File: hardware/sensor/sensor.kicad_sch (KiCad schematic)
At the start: 1 part

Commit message: commit to save work from misbehaving laptop
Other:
- sheet BMS renamed P_{IN}
- sheet Microcontroller ports: added enFrontend; removed none
- sheet Sensor ports: added shutdown; removed none
- moved on the sheet: AE1

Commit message: Fix incorrect upstream
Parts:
- removed AE1: Antenna, symbol Device:Antenna
- added J101: Conn_Coaxial, Connector_Coaxial:SMA_Amphenol_901-143_Horizontal, symbol Connector:Conn_Coaxial
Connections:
- net Microcontroller/Antenna: now also J101.1 (In)
- new net GND: J101.2 (Ext)
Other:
- sheet Microcontroller ports: added LDO_{EN}, V_{ref}, {bms-status}; removed EH_{On}, P_{Good}, V_{Ref}, enFrontend
- sheet P_{IN} ports: added LDO_{EN}, LDO_{OUT}, {bms-status}; removed EH_{On}, P_{Good}
- sheet Reference ports: added V_{ref}; removed V_{Ref}
- sheet Sensor ports: added none; removed shutdown

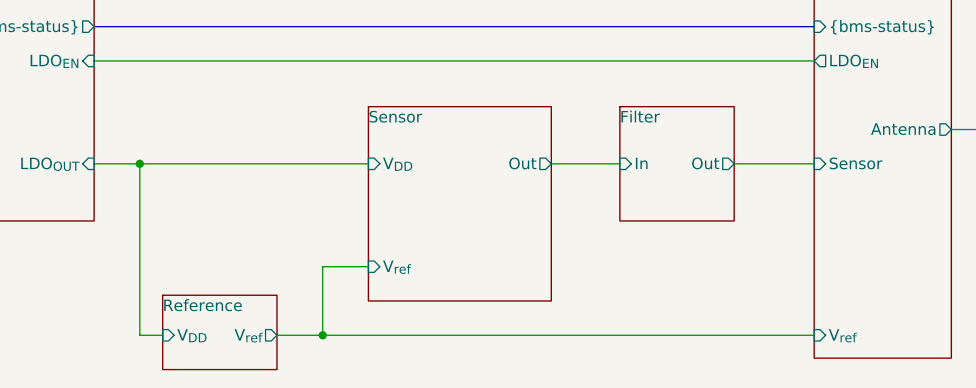
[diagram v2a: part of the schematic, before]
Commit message: Finished initial pcb routing
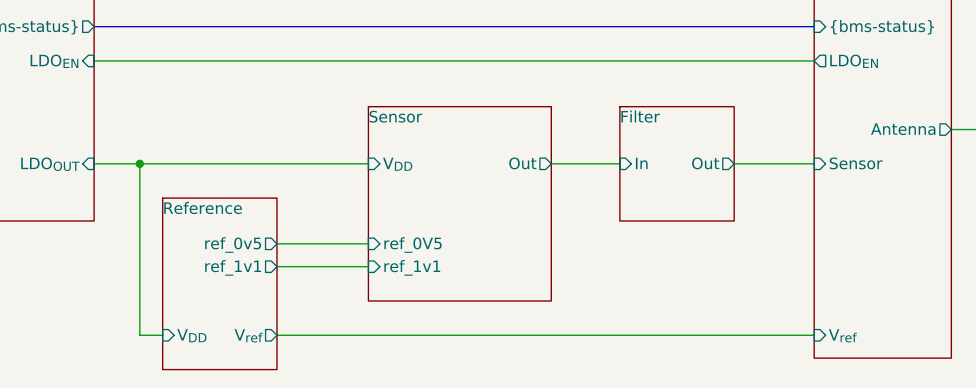
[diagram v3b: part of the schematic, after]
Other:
- sheet Reference ports: added ref_0v5, ref_1v1; removed none
- sheet Sensor ports: added ref_0V5, ref_1v1; removed V_{ref}
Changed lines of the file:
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@@
   (junction (at 59.69 62.23) (diameter 0) (color 0 0 0 0)
-  )
-  (junction (at 80.01 81.28) (diameter 0) (color 0 0 0 0)
   )
   (bus (pts (xy 54.61 46.99) (xy 134.62 46.99))
@@
     (stroke (width 0) (type default))
   )
-  (wire (pts (xy 74.93 81.28) (xy 80.01 81.28))
+  (wire (pts (xy 59.69 62.23) (xy 85.09 62.23))
     (stroke (width 0) (type default))
   )
-  (wire (pts (xy 59.69 62.23) (xy 85.09 62.23))
+  (wire (pts (xy 74.93 81.28) (xy 134.62 81.28))
     (stroke (width 0) (type default))
   )
@@
     (stroke (width 0) (type default))
   )
-  (wire (pts (xy 80.01 81.28) (xy 134.62 81.28))
+  (wire (pts (xy 74.93 71.12) (xy 85.09 71.12))
     (stroke (width 0) (type default))
   )
   (wire (pts (xy 59.69 81.28) (xy 62.23 81.28))
-    (stroke (width 0) (type default))
-  )
-  (wire (pts (xy 80.01 73.66) (xy 80.01 81.28))
     (stroke (width 0) (type default))
   )
@@
     (stroke (width 0) (type default))
   )
-  (wire (pts (xy 80.01 73.66) (xy 85.09 73.66))
+  (wire (pts (xy 74.93 73.66) (xy 85.09 73.66))
     (stroke (width 0) (type default))
   )
@@
     )
   )
-  (sheet (at 62.23 76.835) (size 12.7 8.255)
+  (sheet (at 62.23 66.04) (size 12.7 19.05)
     (stroke (width 0.1524) (type solid))
     (fill (color 0 0 0 0.0000))
-    (property "Sheetname" "Reference" (at 62.23 78.74 0)
+    (property "Sheetname" "Reference" (at 62.23 67.945 0)
       (effects (font (size 1.27 1.27)) (justify left bottom))
     )
-    (property "Sheetfile" "Reference.kicad_sch" (at 62.23 85.6746 0)
+    (property "Sheetfile" "Reference.kicad_sch" (at 62.23 74.8796 0)
       (effects (font (size 1.27 1.27)) (justify left top) hide)
     )
@@
     )
     (pin "V_{ref}" output (at 74.93 81.28 0)
+      (effects (font (size 1.27 1.27)) (justify right))
+    )
+    (pin "ref_0v5" output (at 74.93 71.12 0)
+      (effects (font (size 1.27 1.27)) (justify right))
+    )
+    (pin "ref_1v1" output (at 74.93 73.66 0)
       (effects (font (size 1.27 1.27)) (justify right))
     )
@@
       (effects (font (size 1.27 1.27)) (justify left))
     )
-    (pin "V_{ref}" input (at 85.09 73.66 180)
+    (pin "ref_0V5" input (at 85.09 71.12 180)
       (effects (font (size 1.27 1.27)) (justify left))
     )
+    (pin "ref_1v1" input (at 85.09 73.66 180)
+      (effects (font (size 1.27 1.27)) (justify left))
+    )

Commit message: Add bom and final version of rev 1.0
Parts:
- J101: Digikey (none) -> 931-PCB.114SMAFRAJ.A-ND; Farnell (none) -> 3935093
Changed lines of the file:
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@@
       (effects (font (size 1.27 1.27)) hide)
     )
-    (property "Datasheet" " ~" (at 168.91 58.42 0)
+    (property "Datasheet" "https://www.taoglas.com/datasheets/ConnectorCatalogue.pdf" (at 168.91 58.42 0)
       (effects (font (size 1.27 1.27)) hide)
     )
+    (property "Digikey" "931-PCB.114SMAFRAJ.A-ND" (at 168.91 58.42 0)
+      (effects (font (size 1.27 1.27)) hide)
+    )
+    (property "Farnell" "3935093" (at 168.91 58.42 0)
+      (effects (font (size 1.27 1.27)) hide)
+    )
